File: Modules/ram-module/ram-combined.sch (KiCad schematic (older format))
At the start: 59 parts, among them J1 Conn_01x08, J2 Conn_01x08, J3 Conn_01x10, J4 Conn_01x02, J5 Screw_Terminal_01x02, J6 Conn_01x16, J7 Conn_01x08, J8 Conn_01x08, SW1 SW_SPDT, SW2 SW_Push, SW3 SW_DIP_x08, SW4 SW_DIP_x08, SW5 SW_DIP_x08, U1 74LS00, U10 74LS173, U11 74LS245, U12 74LS173, U13 74LS245, U14 74LS173, U15 74LS157, U16 74LS173, U17 74LS157, U2 74LS32, U3 74LS157, U4 74LS157, U5 74LS173, U6 74LS157, U7 74LS157, U8 74LS173, U9 IS61C1024-15N

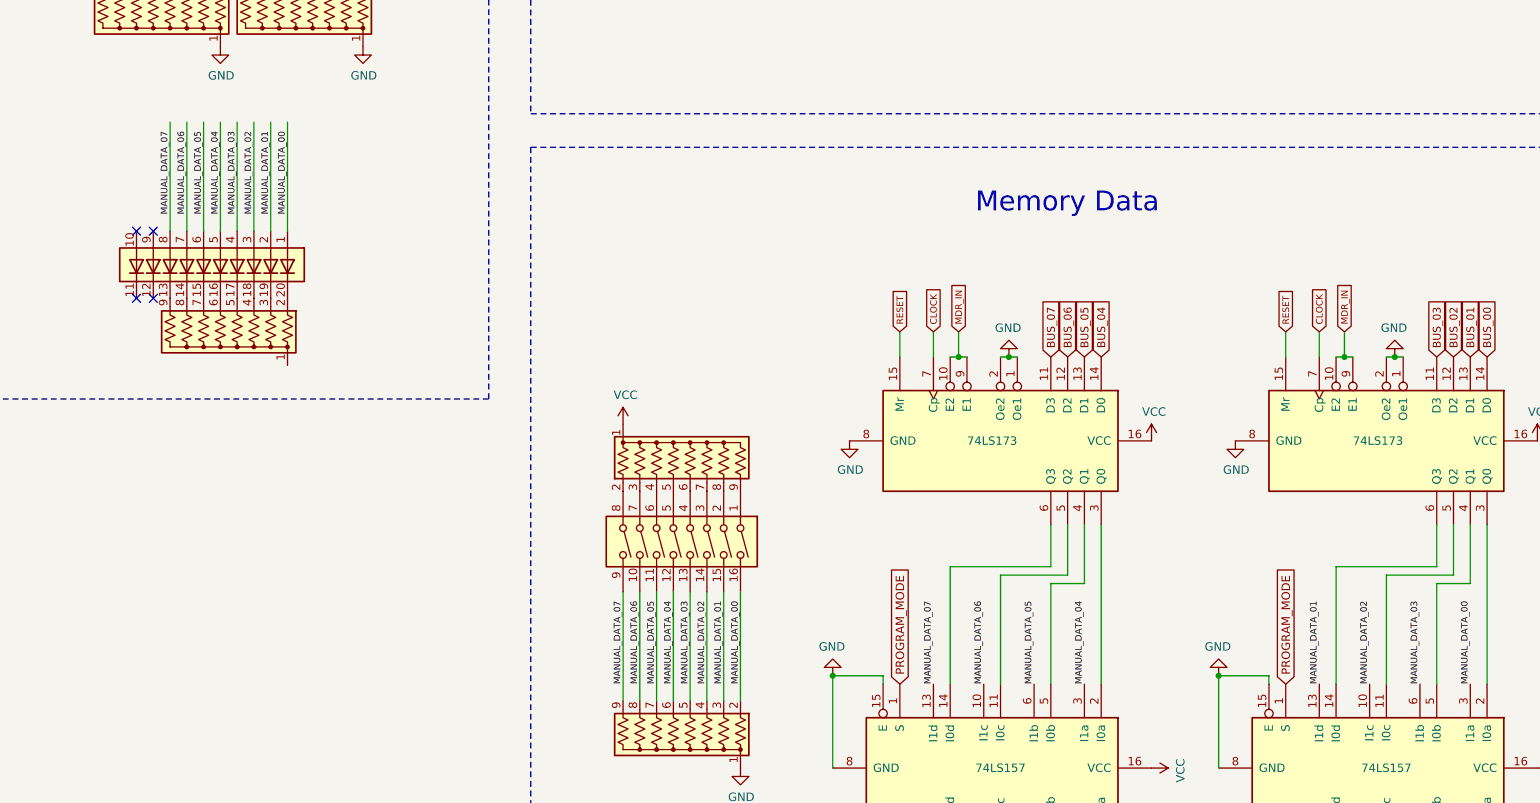
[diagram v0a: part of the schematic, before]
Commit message: [RAM Module] Updates after receiving PCB
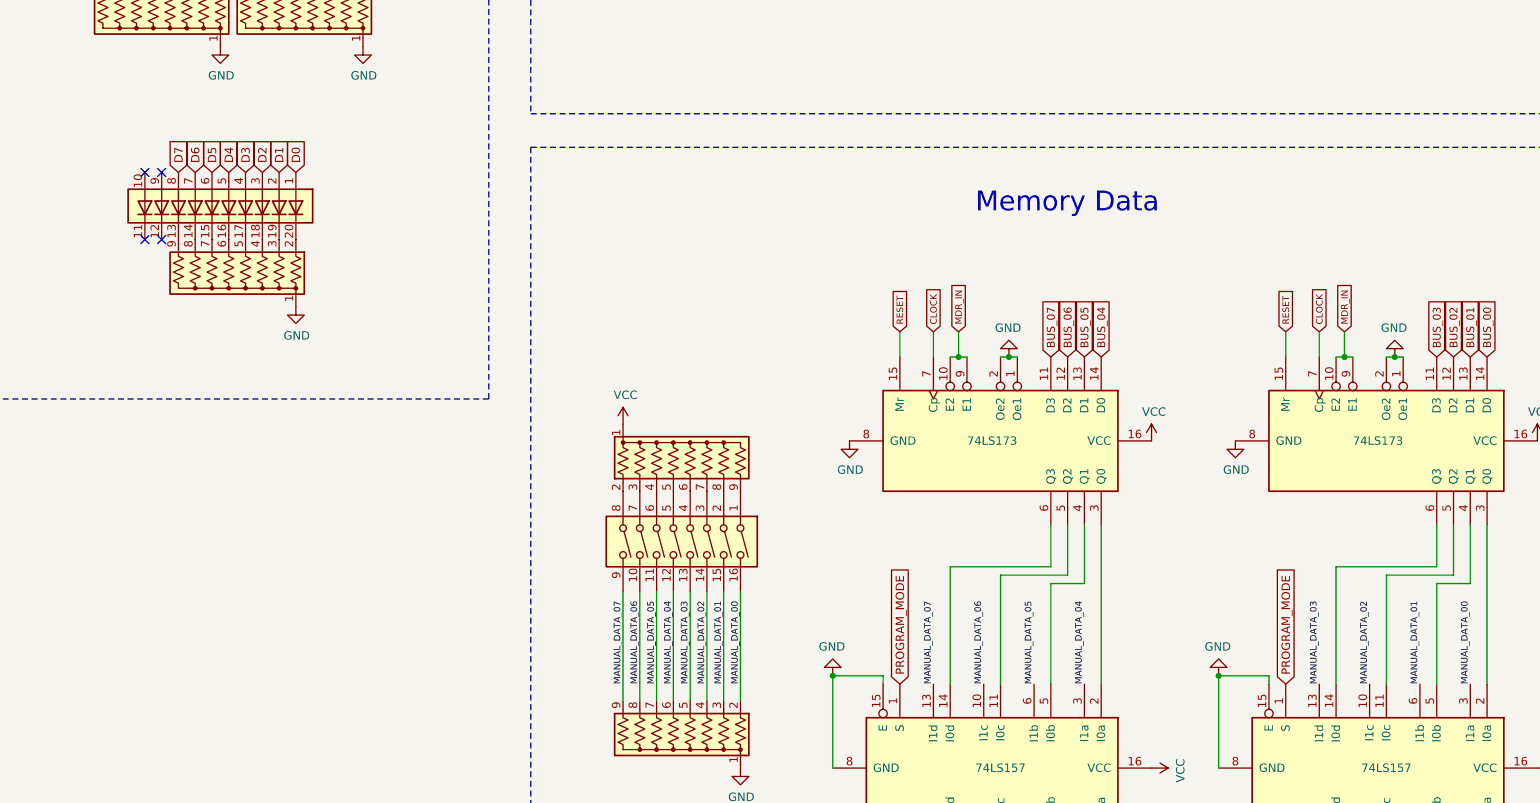
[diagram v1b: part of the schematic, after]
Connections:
- net D0: now also BAR3.1 (A)
- net D1: now also BAR3.2 (A)
- net D2: now also BAR3.3 (A)
- net D3: now also BAR3.4 (A)
- net D4: now also BAR3.5 (A)
- net D5: now also BAR3.6 (A)
- net D6: now also BAR3.7 (A)
- net D7: now also BAR3.8 (A)
- net GND: now also RN10.1 (common)
- net MANUAL_DATA_00: no longer BAR3.1 (A)
- net MANUAL_DATA_01: now also U17.6 (I1b); no longer BAR3.2 (A), U17.13 (I1d)
- net MANUAL_DATA_02: no longer BAR3.3 (A)
- net MANUAL_DATA_03: now also U17.13 (I1d); no longer BAR3.4 (A), U17.6 (I1b)
- net MANUAL_DATA_04: no longer BAR3.5 (A)
- net MANUAL_DATA_05: no longer BAR3.6 (A)
- net MANUAL_DATA_06: no longer BAR3.7 (A)
- net MANUAL_DATA_07: no longer BAR3.8 (A)
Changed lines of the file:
@@
 Text Label 13150 13550 1    39   ~ 0
 MANUAL_DATA_00
-Text Label 12250 13550 1    39   ~ 0
+Text Label 12850 13550 1    39   ~ 0
 MANUAL_DATA_01
 Text Label 12550 13550 1    39   ~ 0
 MANUAL_DATA_02
-Text Label 12850 13550 1    39   ~ 0
+Text Label 12250 13550 1    39   ~ 0
 MANUAL_DATA_03
 Text Label 10850 13550 1    39   ~ 0
@@
 L LED:HDSP-4830_2 BAR3
 U 1 1 638E24AE
-P 5700 11050
-F 0 "BAR3" V 5700 11580 50  0001 L CNN
-F 1 "HDSP-4830_2" V 5745 11580 50  0001 L CNN
-F 2 "Display:HDSP-4830" H 5700 10250 50  0001 C CNN
-F 3 "https://docs.broadcom.com/docs/AV02-1798EN" H 3700 11250 50  0001 C CNN
-	1    5700 11050
+P 5750 10700
+F 0 "BAR3" V 5750 11230 50  0001 L CNN
+F 1 "HDSP-4830_2" V 5795 11230 50  0001 L CNN
+F 2 "Display:HDSP-4830" H 5750 9900 50  0001 C CNN
+F 3 "https://docs.broadcom.com/docs/AV02-1798EN" H 3750 10900 50  0001 C CNN
+	1    5750 10700
 	0    1    1    0
 $EndComp
@@
 L Device:R_Network08_US RN?
 U 1 1 638E55F8
-P 5700 11450
+P 5750 11100
 AR Path="/60C9B792/638E55F8" Ref="RN?"  Part="1"
 AR Path="/638E55F8" Ref="RN10"  Part="1"
-F 0 "RN10" H 5220 11450 50  0001 R CNN
-F 1 "R_Network08_US" H 5220 11495 50  0001 R CNN
-F 2 "Resistor_THT:R_Array_SIP9" V 6175 11450 50  0001 C CNN
-F 3 "http://www.vishay.com/docs/31509/csc.pdf" H 5700 11450 50  0001 C CNN
-	1    5700 11450
+F 0 "RN10" H 5270 11100 50  0001 R CNN
+F 1 "R_Network08_US" H 5270 11145 50  0001 R CNN
+F 2 "Resistor_THT:R_Array_SIP9" V 6225 11100 50  0001 C CNN
+F 3 "http://www.vishay.com/docs/31509/csc.pdf" H 5750 11100 50  0001 C CNN
+	1    5750 11100
 	-1   0    0    1
 $EndComp
-NoConn ~ 5300 11250
-NoConn ~ 5200 11250
-NoConn ~ 5300 10850
-NoConn ~ 5200 10850
-Text Label 6100 10750 1    39   ~ 0
-MANUAL_DATA_00
-Text Label 6000 10750 1    39   ~ 0
-MANUAL_DATA_01
-Text Label 5900 10750 1    39   ~ 0
-MANUAL_DATA_02
-Text Label 5800 10750 1    39   ~ 0
-MANUAL_DATA_03
-Text Label 5700 10750 1    39   ~ 0
-MANUAL_DATA_04
-Text Label 5600 10750 1    39   ~ 0
-MANUAL_DATA_05
-Text Label 5500 10750 1    39   ~ 0
-MANUAL_DATA_06
-Text Label 5400 10750 1    39   ~ 0
-MANUAL_DATA_07
-Wire Wire Line
-	5400 10200 5400 10850
-Wire Wire Line
-	5500 10850 5500 10200
-Wire Wire Line
-	5600 10200 5600 10850
-Wire Wire Line
-	5700 10850 5700 10200
-Wire Wire Line
-	5800 10200 5800 10850
-Wire Wire Line
-	5900 10850 5900 10200
-Wire Wire Line
-	6000 10200 6000 10850
-Wire Wire Line
-	6100 10850 6100 10200
+NoConn ~ 5350 10900
+NoConn ~ 5250 10900
+NoConn ~ 5350 10500
+NoConn ~ 5250 10500
 Text Label 13500 6150 0    50   ~ 0
 A0
@@
 Text Notes 5000 4700 0    50   ~ 10
 SWITCHES
+$Comp
+L power:GND #PWR?
+U 1 1 60E09B61
+P 6150 11300
+AR Path="/60C9B792/60E09B61" Ref="#PWR?"  Part="1"
+AR Path="/60E09B61" Ref="#PWR0115"  Part="1"
+F 0 "#PWR0115" H 6150 11050 50  0001 C CNN
+F 1 "GND" H 6155 11127 50  0000 C CNN
+F 2 "" H 6150 11300 50  0001 C CNN
+F 3 "" H 6150 11300 50  0001 C CNN
+	1    6150 11300
+	1    0    0    -1
+$EndComp
+Text GLabel 6150 10500 1    50   Input ~ 0
+D0
+Text GLabel 6050 10500 1    50   Input ~ 0
+D1
+Text GLabel 5950 10500 1    50   Input ~ 0
+D2
+Text GLabel 5850 10500 1    50   Input ~ 0
+D3
+Text GLabel 5750 10500 1    50   Input ~ 0
+D4
+Text GLabel 5650 10500 1    50   Input ~ 0
+D5
+Text GLabel 5550 10500 1    50   Input ~ 0
+D6
+Text GLabel 5450 10500 1    50   Input ~ 0
+D7
 $EndSCHEMATC
